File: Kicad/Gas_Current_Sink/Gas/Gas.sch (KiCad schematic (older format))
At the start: 13 parts, among them J1 MG811, J2 Digital, J3 MQ135, J4 CCS811, J5 Analog, J6 CONN_01X02, J7 CONN_01X02

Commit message: Gas sensors PCB V1.00a
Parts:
- added D2: LED, LEDs:LED_D4.0mm, symbol LED-RESCUE-Gas
- added R4: R, Resistors_THT:R_Axial_DIN0207_L6.3mm_D2.5mm_P7.62mm_Horizontal, symbol R-RESCUE-Gas
- J1: footprint Pin_Headers:Pin_Header_Straight_1x03_Pitch1.00mm -> Pin_Headers:Pin_Header_Straight_1x03_Pitch2.54mm
- J6, J7: footprint Socket_Strips:Socket_Strip_Angled_1x02_Pitch2.54mm -> Connectors_Molex:Molex_KK-6410-02_02x2.54mm_Straight
- R1, R2, R3: footprint Resistors_THT:R_Axial_DIN0204_L3.6mm_D1.6mm_P5.08mm_Horizontal -> Resistors_THT:R_Axial_DIN0207_L6.3mm_D2.5mm_P7.62mm_Horizontal
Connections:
- net GND: now also D2.1 (K)
- net SCL: now also J2.2; no longer J5.1
- net SDA: now also J2.1; no longer J5.2
- net nINT: now also J2.4; no longer J2.3
- net nRST: now also J5.2; no longer J2.2
- net nWAKE: now also J2.3; no longer J2.4
- net MQ135_out_5v: now reaches J3.2 (P2), R1.1
- net MG811_out: now reaches J1.3 (P3)
- net MG811_out: now also J5.3; no longer J5.4
- net Vout renamed MQ135_out_3V3
- net MQ135_out_3V3: now also J5.4; no longer J5.3
- new net: J5.1, R4.2
- new net: D2.2 (A), R4.1
- no-connect marks 4 -> 2
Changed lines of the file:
@@
 F 0 "R1" V 4830 2050 50  0000 C CNN
 F 1 "6K8" V 4750 2050 50  0000 C CNN
-F 2 "Resistors_THT:R_Axial_DIN0204_L3.6mm_D1.6mm_P5.08mm_Horizontal" V 4680 2050 50  0001 C CNN
+F 2 "Resistors_THT:R_Axial_DIN0207_L6.3mm_D2.5mm_P7.62mm_Horizontal" V 4680 2050 50  0001 C CNN
 F 3 "" H 4750 2050 50  0001 C CNN
 	1    4750 2050
@@
 F 0 "R2" V 4830 2550 50  0000 C CNN
 F 1 "13K2" V 4750 2550 50  0000 C CNN
-F 2 "Resistors_THT:R_Axial_DIN0204_L3.6mm_D1.6mm_P5.08mm_Horizontal" V 4680 2550 50  0001 C CNN
+F 2 "Resistors_THT:R_Axial_DIN0207_L6.3mm_D2.5mm_P7.62mm_Horizontal" V 4680 2550 50  0001 C CNN
 F 3 "" H 4750 2550 50  0001 C CNN
 	1    4750 2550
@@
 $EndComp
 Text GLabel 5150 2300 2    60   Input ~ 0
-Vout
+MQ135_out_3V3
 $Comp
 L CONN_01X04 J1
@@
 F 0 "J1" H 1600 2150 50  0000 C TNN
 F 1 "MG811" V 1650 1850 50  0000 C TNN
-F 2 "Pin_Headers:Pin_Header_Straight_1x03_Pitch1.00mm" H 1600 1425 50  0001 C CNN
+F 2 "Pin_Headers:Pin_Header_Straight_1x03_Pitch2.54mm" H 1600 1425 50  0001 C CNN
 F 3 "" H 1575 2050 50  0001 C CNN
 	1    1600 1850
@@
 F 0 "R3" V 4680 1100 50  0000 C CNN
 F 1 "R" V 4600 1100 50  0000 C CNN
-F 2 "Resistors_THT:R_Axial_DIN0204_L3.6mm_D1.6mm_P5.08mm_Horizontal" V 4530 1100 50  0001 C CNN
+F 2 "Resistors_THT:R_Axial_DIN0207_L6.3mm_D2.5mm_P7.62mm_Horizontal" V 4530 1100 50  0001 C CNN
 F 3 "" H 4600 1100 50  0001 C CNN
 	1    4600 1100
@@
 	0    -1   -1   0
 $EndComp
-Wire Wire Line
-	4750 2200 4750 2400
-Wire Wire Line
-	5500 3350 2350 3350
-Wire Wire Line
-	3750 750  3750 2900
-Connection ~ 4750 2300
-Wire Wire Line
-	1750 2500 3300 2500
-Wire Wire Line
-	4750 1500 4750 1900
-Wire Wire Line
-	4450 1500 4750 1500
-Wire Wire Line
-	4750 3350 4750 2700
-Wire Wire Line
-	1750 1650 2350 1650
-Wire Wire Line
-	2350 1650 2350 3350
-Wire Wire Line
-	3500 2300 5150 2300
-Wire Wire Line
-	5750 1600 4550 1600
-Wire Wire Line
-	5500 1100 5500 3350
-Wire Wire Line
-	1650 1100 4450 1100
-Wire Wire Line
-	1550 1500 1550 1650
-Wire Wire Line
-	4450 1600 4450 1500
-Wire Wire Line
-	5100 1100 5500 1100
-Connection ~ 5500 1600
-Wire Wire Line
-	4800 1100 4750 1100
-Wire Wire Line
-	1650 1100 1650 1650
-Wire Wire Line
-	2350 2800 2050 2800
-Wire Wire Line
-	1950 2800 1950 2700
-Wire Wire Line
-	1950 2700 3750 2700
-Wire Wire Line
-	1850 2800 1850 2600
-Wire Wire Line
-	1850 2600 3400 2600
-Wire Wire Line
-	1750 2800 1750 2500
-Connection ~ 4250 1600
-Wire Wire Line
-	1650 2800 1650 2400
-Wire Wire Line
-	1650 2400 3000 2400
-Connection ~ 2350 2800
-Wire Wire Line
-	1550 2300 2900 2300
-Wire Wire Line
-	1550 2300 1550 2800
-Wire Wire Line
-	1450 2200 2800 2200
-Wire Wire Line
-	1450 2200 1450 2800
-Connection ~ 4750 3350
-Connection ~ 3750 1100
-Wire Wire Line
-	4250 750  4250 1600
-Wire Wire Line
-	3500 2300 3500 2100
-Wire Wire Line
-	3400 2600 3400 2100
-Wire Wire Line
-	3300 2500 3300 2100
-Wire Wire Line
-	3000 2400 3000 2100
-Wire Wire Line
-	2900 2300 2900 2100
-Wire Wire Line
-	2800 2200 2800 2100
-Wire Wire Line
-	4050 3200 4050 3450
-Connection ~ 4050 3350
-Wire Wire Line
-	4050 2900 4050 1600
-Wire Wire Line
-	4050 1600 4250 1600
-Connection ~ 3750 2700
-Wire Wire Line
-	3750 3200 3750 3350
-Connection ~ 3750 3350
-Wire Wire Line
-	1550 1500 3600 1500
-Wire Wire Line
-	3600 1500 3600 2100
 $Comp
 L CONN_01X02 J6
@@
 F 0 "J6" H 6050 1000 50  0000 C CNN
 F 1 "CONN_01X02" V 6150 850 50  0000 C CNN
-F 2 "Socket_Strips:Socket_Strip_Angled_1x02_Pitch2.54mm" H 6050 850 50  0001 C CNN
+F 2 "Connectors_Molex:Molex_KK-6410-02_02x2.54mm_Straight" H 6050 850 50  0001 C CNN
 F 3 "" H 6050 850 50  0001 C CNN
 	1    6050 850
@@
 F 0 "J7" H 6050 1500 50  0000 C CNN
 F 1 "CONN_01X02" V 6150 1350 50  0000 C CNN
-F 2 "Socket_Strips:Socket_Strip_Angled_1x02_Pitch2.54mm" H 6050 1350 50  0001 C CNN
+F 2 "Connectors_Molex:Molex_KK-6410-02_02x2.54mm_Straight" H 6050 1350 50  0001 C CNN
 F 3 "" H 6050 1350 50  0001 C CNN
 	1    6050 1350
 	1    0    0    -1
 $EndComp
+$Comp
+L LED-RESCUE-Gas D2
+U 1 1 599EF3B9
+P 3300 2950
+F 0 "D2" H 3300 3050 50  0000 C CNN
+F 1 "LED" H 3300 2850 50  0000 C CNN
+F 2 "LEDs:LED_D4.0mm" H 3300 2950 50  0001 C CNN
+F 3 "" H 3300 2950 50  0001 C CNN
+	1    3300 2950
+	0    -1   -1   0
+$EndComp
+$Comp
+L R-RESCUE-Gas R4
+U 1 1 599EF44A
+P 3300 2400
+F 0 "R4" V 3380 2400 50  0000 C CNN
+F 1 "R" V 3300 2400 50  0000 C CNN
+F 2 "Resistors_THT:R_Axial_DIN0207_L6.3mm_D2.5mm_P7.62mm_Horizontal" V 3230 2400 50  0001 C CNN
+F 3 "" H 3300 2400 50  0001 C CNN
+	1    3300 2400
+	-1   0    0    1
+$EndComp
+Wire Wire Line
+	4750 2200 4750 2400
+Wire Wire Line
+	5500 3350 2350 3350
+Wire Wire Line
+	3750 750  3750 2900
+Connection ~ 4750 2300
+Wire Wire Line
+	1750 2500 2800 2500
+Wire Wire Line
+	4750 1500 4750 1900
+Wire Wire Line
+	4450 1500 4750 1500
+Wire Wire Line
+	4750 3350 4750 2700
+Wire Wire Line
+	1750 1650 2350 1650
+Wire Wire Line
+	2350 1650 2350 3350
+Wire Wire Line
+	3600 2300 5150 2300
+Wire Wire Line
+	5750 1600 4550 1600
+Wire Wire Line
+	5500 1100 5500 3350
+Wire Wire Line
+	1650 1100 4450 1100
+Wire Wire Line
+	1550 1500 1550 1650
+Wire Wire Line
+	4450 1600 4450 1500
+Wire Wire Line
+	5100 1100 5500 1100
+Connection ~ 5500 1600
+Wire Wire Line
+	4800 1100 4750 1100
+Wire Wire Line
+	1650 1100 1650 1650
+Wire Wire Line
+	2350 2800 2050 2800
+Wire Wire Line
+	1950 2800 1950 2700
+Wire Wire Line
+	1950 2700 3750 2700
+Wire Wire Line
+	1850 2800 1850 2600
+Wire Wire Line
+	1850 2600 2700 2600
+Wire Wire Line
+	1750 2800 1750 2500
+Connection ~ 4250 1600
+Wire Wire Line
+	1650 2800 1650 2400
+Wire Wire Line
+	1650 2400 2900 2400
+Connection ~ 2350 2800
+Wire Wire Line
+	1550 2300 3000 2300
+Wire Wire Line
+	1550 2300 1550 2800
+Wire Wire Line
+	1450 2200 3400 2200
+Wire Wire Line
+	1450 2200 1450 2800
+Connection ~ 4750 3350
+Connection ~ 3750 1100
+Wire Wire Line
+	4250 750  4250 1600
+Wire Wire Line
+	3600 2300 3600 2100
+Wire Wire Line
+	2900 2400 2900 2100
+Wire Wire Line
+	3000 2300 3000 2100
+Wire Wire Line
+	4050 3200 4050 3450
+Connection ~ 4050 3350
+Wire Wire Line
+	4050 2900 4050 1600
+Wire Wire Line
+	4050 1600 4250 1600
+Connection ~ 3750 2700
+Wire Wire Line
+	3750 3200 3750 3350
+Connection ~ 3750 3350
+Wire Wire Line
+	1550 1500 3500 1500
+Wire Wire Line
+	3500 1500 3500 2100
 Wire Wire Line
 	5850 800  3750 800
@@
 	5750 1400 5850 1400
 Connection ~ 5750 1400
-NoConn ~ 2700 2100
-NoConn ~ 3000 1950
+Wire Wire Line
+	2700 2600 2700 2100
+Wire Wire Line
+	2800 2500 2800 2100
+Wire Wire Line
+	3400 2200 3400 2100
+Wire Wire Line
+	3300 2800 3300 2550
+Wire Wire Line
+	3300 2250 3300 2100
+Wire Wire Line
+	3300 3100 3300 3350
+Connection ~ 3300 3350
+Text Label 1950 1500 0    60   ~ 0
+MG811_out
+Text Label 4450 1500 0    60   ~ 0
+MQ135_out_5v
 $EndSCHEMATC

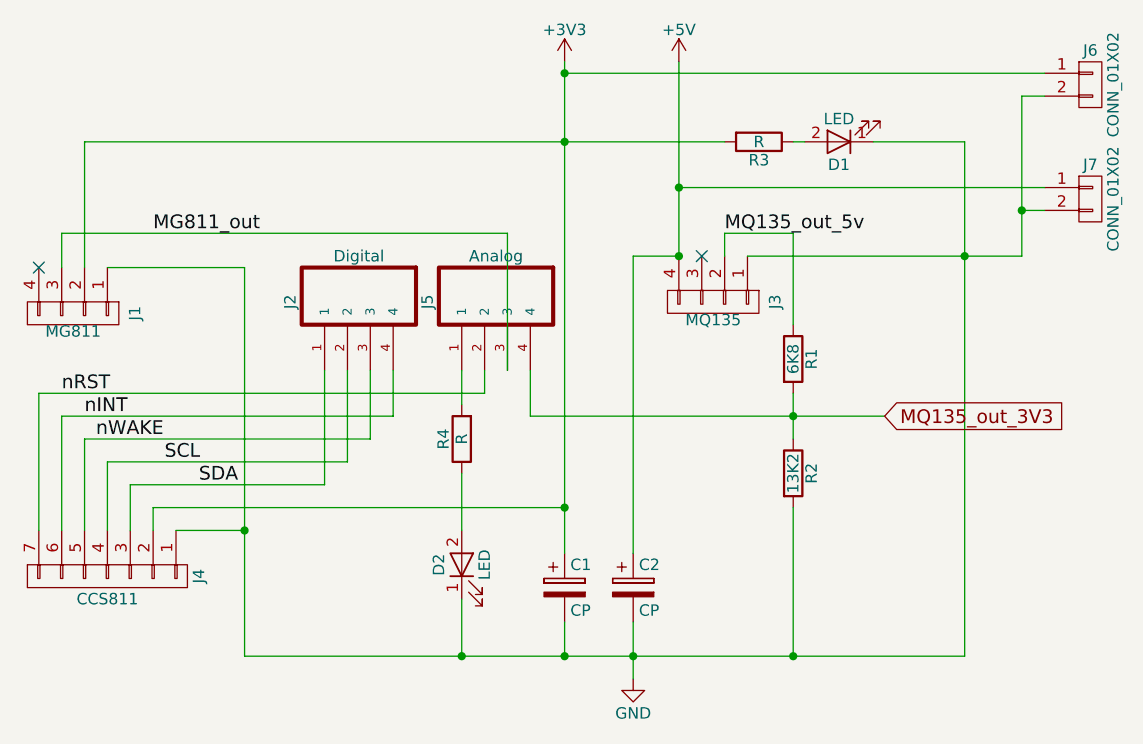
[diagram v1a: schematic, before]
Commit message: Current and CO2 Arduino and Kicad Release 1.00! Added Arduino code for CO2 and Current sensor module. Updated Kicad projects for Arduino Due shield and top of the box CO2 PCB.
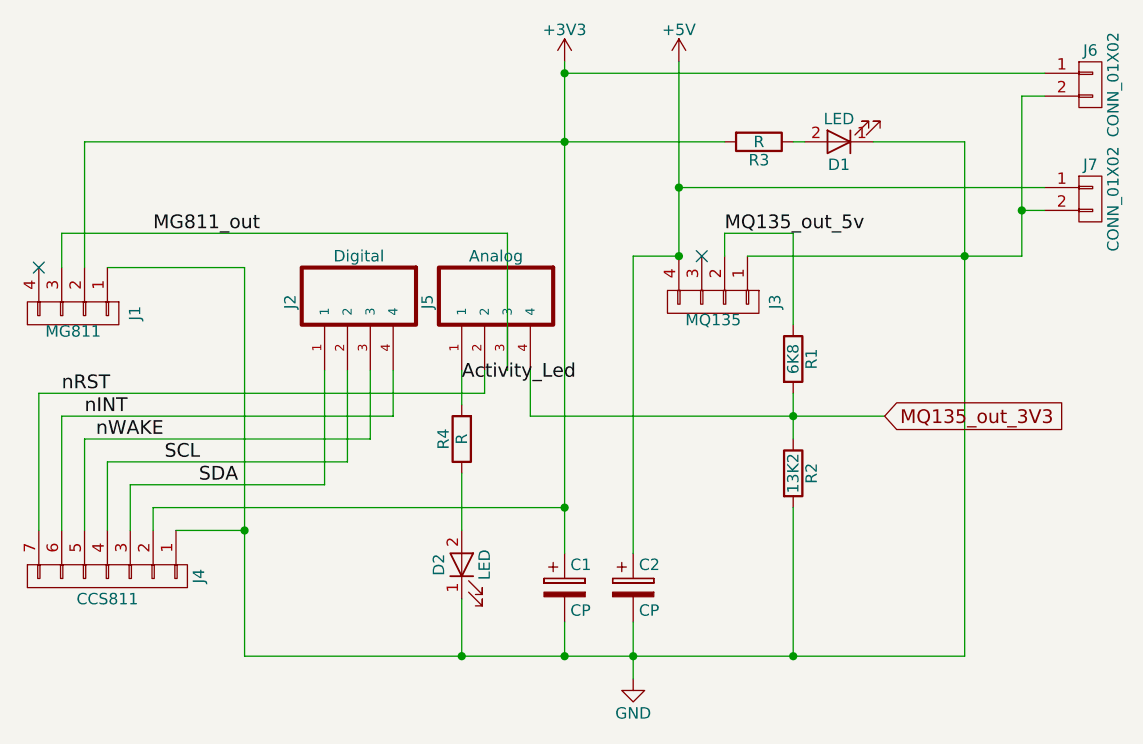
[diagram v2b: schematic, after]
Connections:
- net Activity_Led: now reaches J5.1, R4.2
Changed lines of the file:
@@
 Text Label 4450 1500 0    60   ~ 0
 MQ135_out_5v
+Text Label 3300 2150 0    60   ~ 0
+Activity_Led
 $EndSCHEMATC
